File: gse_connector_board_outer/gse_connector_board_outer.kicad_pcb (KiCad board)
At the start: 2 copper layers, 52 x 27 mm, 9 parts, among them J1 arming_connector, J2 gse_com_connector, J3 chg_connector, J5 Conn_02x02_Top_Bottom, J6 Conn_02x02_Top_Bottom, J7 Conn_02x02_Top_Bottom

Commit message: cleanup silkscreen
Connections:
- J5 pad 2: disarm -> arm
- J5 pad 4: arm -> disarm
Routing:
- net arm: track 17.5 -> 22.7 mm
- net CHG: track 15.7 -> 19.8 mm
- net disarm: track 21.0 -> 19.0 mm
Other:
- board text added: "rev2"
- board text removed: "rev1"
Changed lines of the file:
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@@
 			(layers "*.Cu" "*.Mask")
 			(remove_unused_layers no)
-			(net "disarm")
+			(net "arm")
 			(pinfunction "Pin_2_2")
 			(pintype "passive")
@@
 			(layers "*.Cu" "*.Mask")
 			(remove_unused_layers no)
-			(net "arm")
+			(net "disarm")
 			(pinfunction "Pin_4_4")
 			(pintype "passive")
@@
 		)
 	)
-	(gr_text "rev1\n"
+	(gr_text "rev2"
 		(at 129.955256 89.991018 0)
 		(layer "F.SilkS")
@@
 	)
 	(gr_text "d.arm\n"
-		(at 130.05 97.45 0)
+		(at 130.4 100.55 0)
 		(layer "F.SilkS")
 		(effects
@@
 	)
 	(gr_text "arm"
-		(at 131.65 100.65 0)
+		(at 131.725 97.5 0)
 		(layer "F.SilkS")
 		(effects
@@
 	)
 	(segment
-		(start 129.3 105.3)
-		(end 129.3 108)
+		(start 123.5 97.085)
+		(end 124.96 98.545)
 		(width 0.5)
 		(layer "F.Cu")
@@
 	)
 	(segment
-		(start 123.5 97.085)
-		(end 124.825256 98.410256)
+		(start 128.781018 104.781018)
+		(end 129.85 105.85)
 		(width 0.5)
 		(layer "F.Cu")
@@
 	)
 	(segment
-		(start 128.781018 104.781018)
-		(end 129.3 105.3)
+		(start 124.96 98.545)
+		(end 124.96 102.915762)
 		(width 0.5)
 		(layer "F.Cu")
@@
 	)
 	(segment
-		(start 124.825256 102.781018)
+		(start 129.85 105.85)
+		(end 129.85 108)
+		(width 0.5)
+		(layer "F.Cu")
+		(net "+V_EXT")
+	)
+	(segment
+		(start 124.96 102.915762)
 		(end 126.825256 104.781018)
 		(width 0.5)
@@
 		(start 126.825256 104.781018)
 		(end 128.781018 104.781018)
-		(width 0.5)
-		(layer "F.Cu")
-		(net "+V_EXT")
-	)
-	(segment
-		(start 124.825256 98.410256)
-		(end 124.825256 102.781018)
 		(width 0.5)
 		(layer "F.Cu")
@@
 	)
 	(segment
-		(start 135.5 100.3)
-		(end 137.6 102.4)
+		(start 134.11 98.475)
+		(end 135.5 97.085)
 		(width 0.5)
 		(layer "F.Cu")
@@
 	)
 	(segment
+		(start 146.75 108)
+		(end 146.75 103.2)
+		(width 0.5)
+		(layer "F.Cu")
+		(net "arm")
+	)
+	(segment
+		(start 135.725 102.4)
+		(end 134.11 100.785)
+		(width 0.5)
+		(layer "F.Cu")
+		(net "arm")
+	)
+	(segment
+		(start 134.11 100.785)
+		(end 134.11 98.475)
+		(width 0.5)
+		(layer "F.Cu")
+		(net "arm")
+	)
+	(segment
 		(start 146.75 103.2)
-		(end 146.75 108)
+		(end 145.95 102.4)
 		(width 0.5)
 		(layer "F.Cu")
@@
 	(segment
 		(start 145.95 102.4)
-		(end 146.75 103.2)
+		(end 135.725 102.4)
 		(width 0.5)
 		(layer "F.Cu")
@@
 	)
 	(segment
-		(start 137.6 102.4)
-		(end 145.95 102.4)
-		(width 0.5)
-		(layer "F.Cu")
-		(net "arm")
+		(start 135.5 100.085)
+		(end 136.865 101.45)
+		(width 0.5)
+		(layer "F.Cu")
+		(net "disarm")
+	)
+	(segment
+		(start 136.865 101.45)
+		(end 138.167943 101.45)
+		(width 0.5)
+		(layer "F.Cu")
+		(net "disarm")
+	)
+	(segment
+		(start 138.167943 101.45)
+		(end 146.6 101.45)
+		(width 0.5)
+		(layer "F.Cu")
+		(net "disarm")
+	)
+	(segment
+		(start 148 102.85)
+		(end 148 108)
+		(width 0.5)
+		(layer "F.Cu")
+		(net "disarm")
+	)
+	(segment
+		(start 146.6 101.45)
+		(end 148 102.85)
+		(width 0.5)
+		(layer "F.Cu")
+		(net "disarm")
 	)
 	(segment
@@
 		(width 0.5)
 		(layer "F.Cu")
-		(net "arm")
-	)
-	(segment
-		(start 135.5 97.085)
-		(end 137.05 98.635)
-		(width 0.5)
-		(layer "F.Cu")
 		(net "disarm")
 	)
 	(segment
-		(start 138.167943 101.45)
-		(end 146.6 101.45)
-		(width 0.5)
-		(layer "F.Cu")
-		(net "disarm")
-	)
-	(segment
-		(start 137.05 98.635)
-		(end 137.05 100.332057)
-		(width 0.5)
-		(layer "F.Cu")
-		(net "disarm")
-	)
-	(segment
-		(start 148 102.85)
-		(end 148 108)
-		(width 0.5)
-		(layer "F.Cu")
-		(net "disarm")
-	)
-	(segment
-		(start 146.6 101.45)
-		(end 148 102.85)
-		(width 0.5)
-		(layer "F.Cu")
-		(net "disarm")
-	)
-	(segment
-		(start 137.05 100.332057)
-		(end 138.167943 101.45)
-		(width 0.5)
-		(layer "F.Cu")
-		(net "disarm")
+		(start 117.56 105.210512)
+		(end 117.3 104.950512)
+		(width 1)
+		(layer "F.Cu")
+		(net "CHG")
+	)
+	(segment
+		(start 117.084744 104.735256)
+		(end 117.084744 107.084744)
+		(width 1)
+		(layer "F.Cu")
+		(net "CHG")
 	)
 	(segment
@@
 	)
 	(segment
-		(start 116.5 105.750512)
-		(end 117.3 104.950512)
+		(start 116.159744 103.810256)
+		(end 116.949744 104.600256)
 		(width 1)
 		(layer "F.Cu")
@@
 	)
 	(segment
-		(start 118 105.650512)
+		(start 117.56 105.210512)
+		(end 117.56 106.32)
+		(width 1)
+		(layer "F.Cu")
+		(net "CHG")
+	)
+	(segment
+		(start 117.084744 107.665256)
+		(end 116.75 108)
+		(width 1)
+		(layer "F.Cu")
+		(net "CHG")
+	)
+	(segment
+		(start 117.084744 104.735256)
+		(end 117.084744 107.665256)
+		(width 1)
+		(layer "F.Cu")
+		(net "CHG")
+	)
+	(segment
+		(start 117.084744 107.084744)
 		(end 118 108)
 		(width 1)
@@
 	)
 	(segment
-		(start 117.3 104.950512)
-		(end 118 105.650512)
+		(start 117.56 106.32)
+		(end 117.21 106.67)
 		(width 1)
 		(layer "F.Cu")
@@
 	)
 	(segment
-		(start 116.5 108)
-		(end 116.5 105.750512)
+		(start 116.949744 104.600256)
+		(end 117.084744 104.735256)
+		(width 1)
+		(layer "F.Cu")
+		(net "CHG")
+	)
+	(segment
+		(start 116.949744 104.600256)
+		(end 117.3 104.950512)
 		(width 1)
 		(layer "F.Cu")
@@
 		(polygon
 			(pts
-				(xy 121.625256 95.581018) (xy 128.825247 95.581018) (xy 137.585248 104.341) (xy 137.585256 112.181018)
-				(xy 127.025256 112.181018) (xy 127.025256 108.781018) (xy 121.625256 103.381018)
-			)
-		)
+				(xy 121.625256 95.581018) (xy 127.8 95.52) (xy 137.625 105.15) (xy 137.585256 112.181018) (xy 127.025256 112.181018)
+				(xy 127.025256 108.781018) (xy 121.625256 103.381018)
+			)
+		)

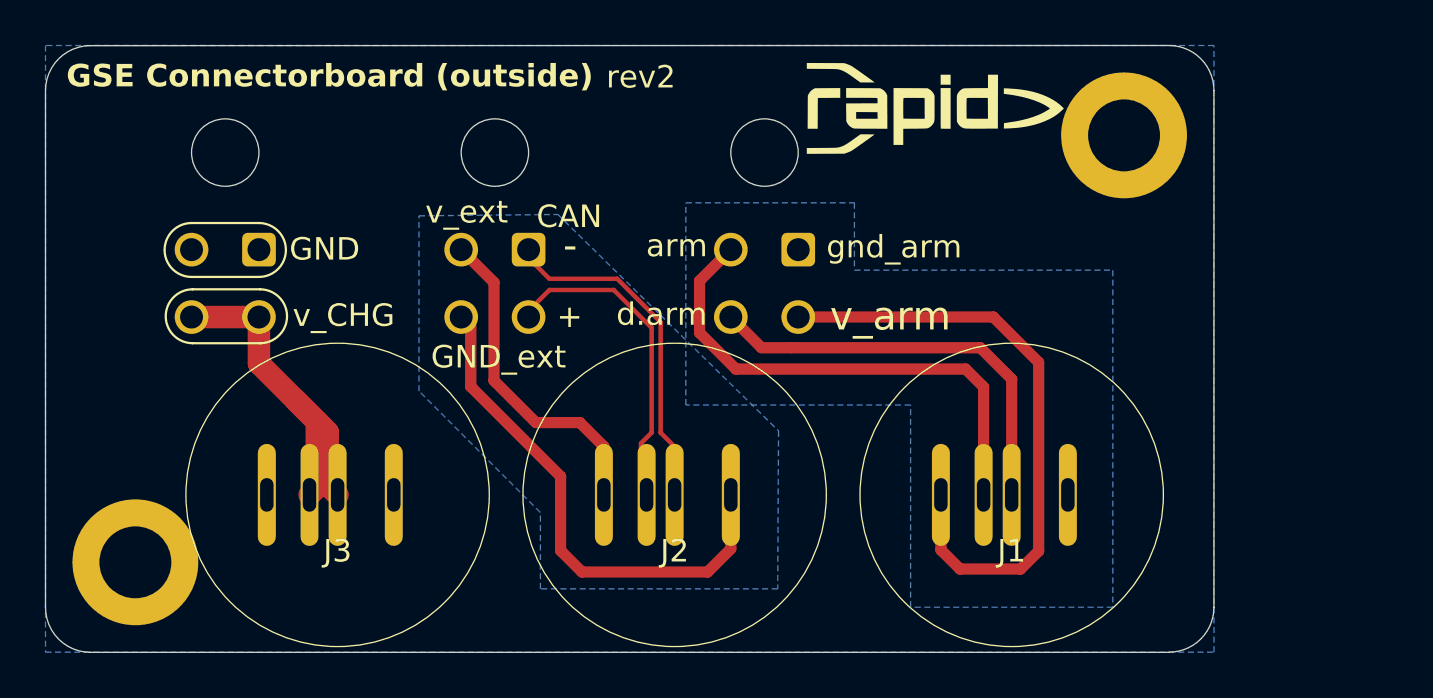
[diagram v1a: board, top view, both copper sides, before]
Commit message: fix connector pinout
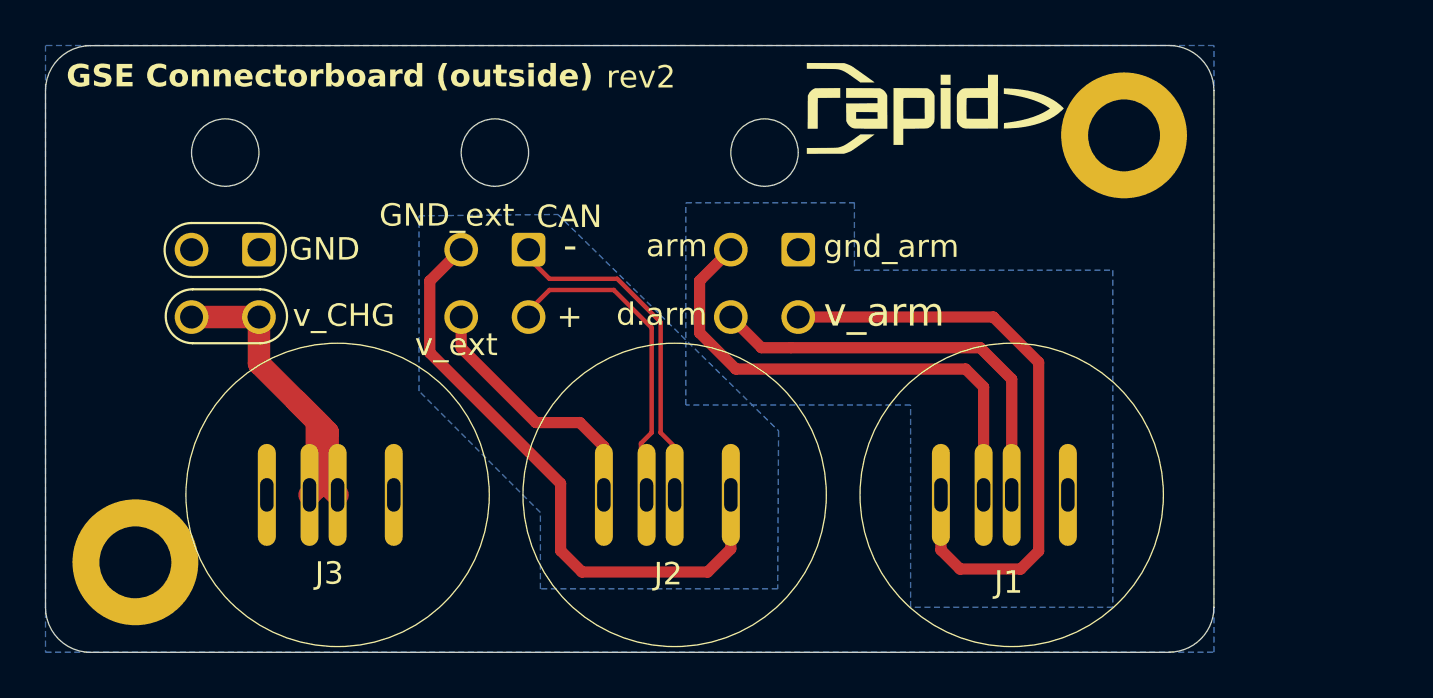
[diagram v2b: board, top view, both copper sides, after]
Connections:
- J6 pad 2: +V_EXT -> GND_EXT
- J6 pad 4: GND_EXT -> +V_EXT
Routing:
- net GND_EXT: track 23.0 -> 27.2 mm
- net +V_EXT: track 14.7 -> 11.7 mm
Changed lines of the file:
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@@
 		(at 133 111)
 		(property "Reference" "J2"
-			(at 0 -0.5 0)
+			(at -0.29 0.52 0)
 			(unlocked yes)
 			(layer "F.SilkS")
@@
 		(at 148 111)
 		(property "Reference" "J1"
-			(at 0 -0.5 0)
+			(at -0.14 0.89 0)
 			(unlocked yes)
 			(layer "F.SilkS")
@@
 		(at 118 111)
 		(property "Reference" "J3"
-			(at 0 -0.5 0)
+			(at -0.37 0.49 0)
 			(unlocked yes)
 			(layer "F.SilkS")
@@
 			(layers "*.Cu" "*.Mask")
 			(remove_unused_layers no)
-			(net "+V_EXT")
+			(net "GND_EXT")
 			(pinfunction "Pin_2_2")
 			(pintype "passive")
@@
 			(layers "*.Cu" "*.Mask")
 			(remove_unused_layers no)
-			(net "GND_EXT")
+			(net "+V_EXT")
 			(pinfunction "Pin_4_4")
 			(pintype "passive")
@@
 		)
 	)
-	(gr_text "v_ext"
-		(at 121.9 96 0)
+	(gr_text "GND_ext\n"
+		(at 119.85 96.14 0)
 		(layer "F.SilkS")
 		(effects
@@
 		)
 	)
-	(gr_text "GND_ext\n"
-		(at 122.15 102.45 0)
+	(gr_text "v_ext"
+		(at 121.44 101.9 0)
 		(layer "F.SilkS")
 		(effects
@@
 	)
 	(gr_text "gnd_arm"
-		(at 139.75 97.55 0)
+		(at 139.62 97.53 0)
 		(layer "F.SilkS")
 		(effects
@@
 	)
 	(gr_text "v_arm"
-		(at 142.6 100.05 0)
+		(at 142.32 99.88 0)
 		(layer "F.SilkS")
 		(effects
@@
 	)
 	(segment
-		(start 123.5 97.085)
-		(end 124.96 98.545)
+		(start 129.85 105.85)
+		(end 129.85 108)
 		(width 0.5)
 		(layer "F.Cu")
@@
 	)
 	(segment
-		(start 124.96 98.545)
-		(end 124.96 102.915762)
-		(width 0.5)
-		(layer "F.Cu")
-		(net "+V_EXT")
-	)
-	(segment
-		(start 129.85 105.85)
-		(end 129.85 108)
-		(width 0.5)
-		(layer "F.Cu")
-		(net "+V_EXT")
-	)
-	(segment
-		(start 124.96 102.915762)
-		(end 126.825256 104.781018)
-		(width 0.5)
-		(layer "F.Cu")
-		(net "+V_EXT")
-	)
-	(segment
 		(start 126.825256 104.781018)
 		(end 128.781018 104.781018)
+		(width 0.5)
+		(layer "F.Cu")
+		(net "+V_EXT")
+	)
+	(segment
+		(start 123.5 100.085)
+		(end 123.5 101.455762)
+		(width 0.5)
+		(layer "F.Cu")
+		(net "+V_EXT")
+	)
+	(segment
+		(start 123.5 101.455762)
+		(end 126.825256 104.781018)
 		(width 0.5)
 		(layer "F.Cu")
@@
 	)
 	(segment
+		(start 127.925256 110.481018)
+		(end 127.925256 107.495256)
+		(width 0.5)
+		(layer "F.Cu")
+		(net "GND_EXT")
+	)
+	(segment
+		(start 128.875256 111.431018)
+		(end 127.925256 110.481018)
+		(width 0.5)
+		(layer "F.Cu")
+		(net "GND_EXT")
+	)
+	(segment
+		(start 122.1 101.67)
+		(end 122.1 98.485)
+		(width 0.5)
+		(layer "F.Cu")
+		(net "GND_EXT")
+	)
+	(segment
+		(start 122.1 98.485)
+		(end 123.5 97.085)
+		(width 0.5)
+		(layer "F.Cu")
+		(net "GND_EXT")
+	)
+	(segment
 		(start 135.5 110.403137)
-		(end 135.5 108)
-		(width 0.5)
-		(layer "F.Cu")
-		(net "GND_EXT")
-	)
-	(segment
-		(start 123.5 100.085)
-		(end 123.925256 100.510256)
-		(width 0.5)
-		(layer "F.Cu")
-		(net "GND_EXT")
-	)
-	(segment
-		(start 123.925256 100.510256)
-		(end 123.925256 103.181018)
+		(end 134.472119 111.431018)
 		(width 0.5)
 		(layer "F.Cu")
@@
 	(segment
 		(start 134.472119 111.431018)
+		(end 128.875256 111.431018)
+		(width 0.5)
+		(layer "F.Cu")
+		(net "GND_EXT")
+	)
+	(segment
+		(start 135.5 108)
 		(end 135.5 110.403137)
 		(width 0.5)
@@
 	)
 	(segment
-		(start 127.925256 107.181018)
-		(end 127.925256 110.481018)
+		(start 127.925256 107.495256)
+		(end 122.1 101.67)
 		(width 0.5)
 		(layer "F.Cu")
-		(net "GND_EXT")
-	)
-	(segment
-		(start 127.925256 110.481018)
-		(end 128.875256 111.431018)
-		(width 0.5)
-		(layer "F.Cu")
-		(net "GND_EXT")
-	)
-	(segment
-		(start 128.875256 111.431018)
-		(end 134.472119 111.431018)
-		(width 0.5)
-		(layer "F.Cu")
-		(net "GND_EXT")
-	)
-	(segment
-		(start 123.925256 103.181018)
-		(end 127.925256 107.181018)
-		(width 0.5)
-		(layer "F.Cu")

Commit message: route new can isolation
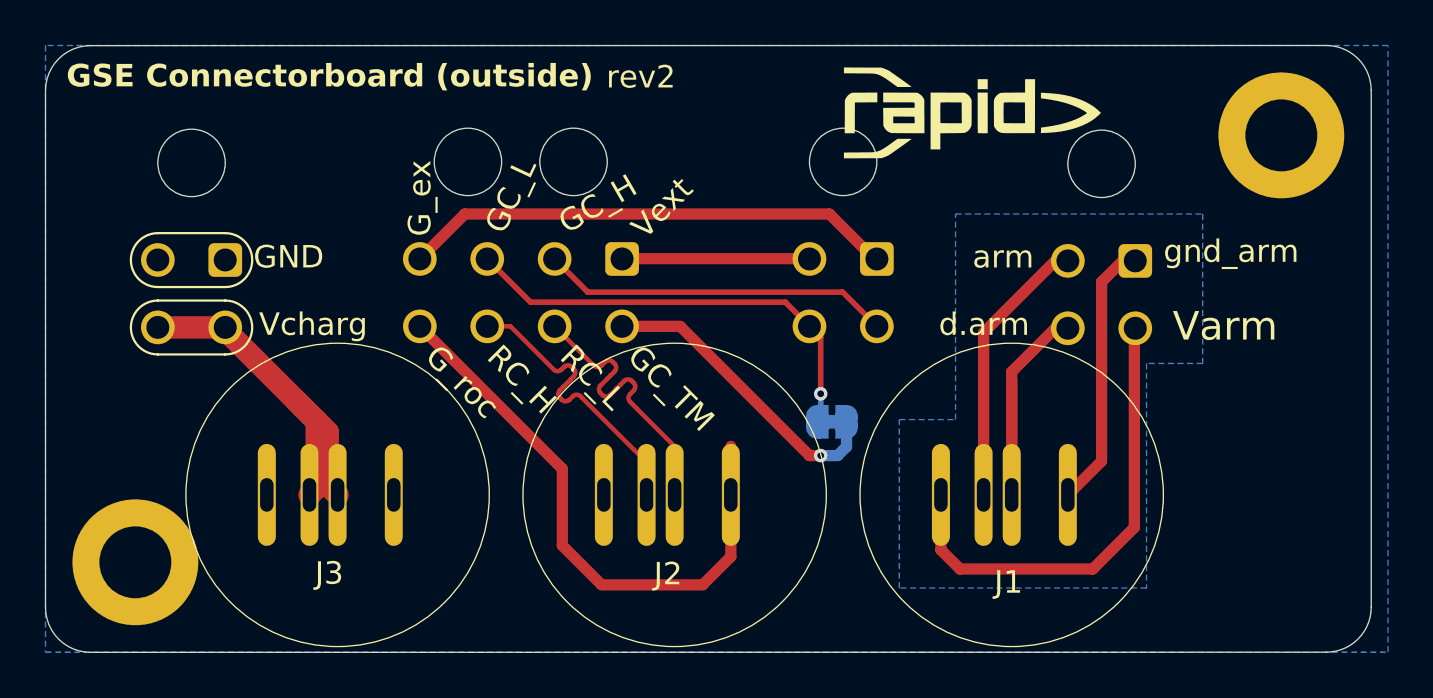
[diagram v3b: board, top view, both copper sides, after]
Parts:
- removed J6: Conn_02x02_Top_Bottom, Connector_Molex:Molex_Micro-Fit_3.0_43045-0400_2x02_P3.00mm_Horizontal
- added 120Ω: SolderJumper_2_Bridged, Jumper:SolderJumper-2_P1.3mm_Bridged_RoundedPad1.0x1.5mm, B.Cu at (140.0, 104.8)
- added J4: Conn_02x04_Top_Bottom, Connector_Molex:Molex_Micro-Fit_3.0_43045-0800_2x04_P3.00mm_Horizontal, B.Cu at (130.7, 97.5)
- added J8: Conn_02x02_Top_Bottom, Connector_Molex:Molex_Micro-Fit_3.0_43045-0400_2x02_P3.00mm_Horizontal, B.Cu at (142.0, 97.5)
- moved J5 15.0 mm to (153.5, 97.6)
- moved H2 7.00 mm to (160.0, 92.0)
- moved G*** 1.66 mm to (146.2, 91.0)
- moved J7 1.57 mm to (113.0, 97.5)
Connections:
- J2 pad 1: +V_EXT -> unconnected-(J2-Pin_1-Pad1)
- J2 pad 2: CAN_ext+ -> CAN_rocket_H
- J2 pad 3: CAN_ext- -> CAN_rocket_L
- J2 pad 4: GND_EXT -> GND_rocket
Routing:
- net GND_rocket: track 0.00 -> 26.0 mm
- net GSE_CANL: track 0.00 -> 20.1 mm, vias 0 -> 1
- net GSE_CANH: track 0.00 -> 15.6 mm
- net CAN_ext+: track 14.3 -> 0.00 mm
- net GSE_CAN_TERM: track 0.00 -> 14.0 mm, vias 0 -> 1
- net CAN_rocket_H: track 0.00 -> 13.1 mm
- net CAN_rocket_L: track 0.00 -> 13.0 mm
- net CAN_ext-: track 12.9 -> 0.00 mm
- net GND_Arm: track 0.00 -> 11.5 mm
- net arm: track 22.7 -> 11.8 mm
- net Voltage_Arm: track 27.4 -> 21.1 mm
- net disarm: track 19.0 -> 13.5 mm
- net GND_EXT: track 27.2 -> 22.0 mm
- net +V_EXT: track 11.7 -> 7.85 mm
- removed copper zone on B.Cu, net GND_EXT
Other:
- board size 52 x 27 mm -> 59 x 27 mm
- board text added: "GC_H"
- board text added: "GC_L"
- board text added: "GC_TM"
- board text added: "G_ex"
- board text added: "G_roc"
- board text added: "RC_H"
- board text added: "RC_L"
- board text added: "Varm"
- board text added: "Vcharg"
- board text added: "Vext"
- board text removed: "+"
- board text removed: "-"
- board text removed: "CAN"
- board text removed: "v_CHG"
- board text removed: "v_arm"
- board text removed: "v_ext"

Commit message: adapted footprint again
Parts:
- J1, J2, J3: footprint custom_parts:4_pin_mag_con_new -> custom_parts:4_pin_mag_con_mv_adapt
- renumbered 120Ω to JP1
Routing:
- net GND_EXT: track 22.0 -> 0.11 mm
- net CHG: track 20.1 -> 0.00 mm
- net GND_Arm: track 11.5 -> 0.00 mm
- net GND_rocket: track 26.0 -> 23.9 mm
- added copper zone on F.Cu, net CHG
- added copper zone on B.Cu, net GND_EXT
